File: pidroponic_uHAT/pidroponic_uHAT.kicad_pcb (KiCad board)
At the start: 2 copper layers, 65 x 30 mm, 28 parts, among them J1 GPIO_CONNECTOR, J2 1935161, J3 B4B-PH-K-S_LF__SN_, J4 B4B-PH-K-S_LF__SN_, J5 B4B-PH-K-S_LF__SN_, J6 B6B-PH-K-S_LF__SN_, J7 B4B-PH-K-S_LF__SN_, J8 TI ADS1115 Breakout, J9 B4B-PH-K-S_LF__SN_, Q1 DMG2305UX-13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

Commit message: updates over the last few evenings.
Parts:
- J2: footprint digikey-footprints:Terminal_Block_D1.3mm_P5mm -> TerminalBlock_Phoenix:TerminalBlock_Phoenix_PT-1,5-2-5.0-H_1x02_P5.00mm_Horizontal
- moved U1 10.8 mm to (133.5, 108.3)
- moved Q1 5.81 mm to (137.5, 112.6)
- moved C1 4.66 mm to (128.9, 107.3)
- moved C2 4.64 mm to (128.9, 104.0)
- moved J2 1.27 mm to (122.0, 108.8)
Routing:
- net GND: track 15.5 -> 32.1 mm, vias 1 -> 0
- net Net-(C2-Pad1): track 21.1 -> 32.1 mm
- net Net-(Q1-Pad1): track 8.00 -> 15.7 mm
- net /P12V: track 23.5 -> 17.3 mm
- net +5V: track 98.7 -> 101.7 mm
- net +3V3: track 90.4 -> 92.6 mm
- net /GPIO2_SDA1: track 35.0 -> 37.0 mm, vias 2 -> 0
- net /GPIO3_SCL1: track 35.0 -> 37.0 mm, vias 0 -> 1
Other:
- board text added: "4/27/2020 - Bryan Varner"
- board text added: "Pidroponics 1.0.8"
- board text removed: "4/23/2020 - Bryan Varner"
- board text removed: "Pidroponics 1.0.7"

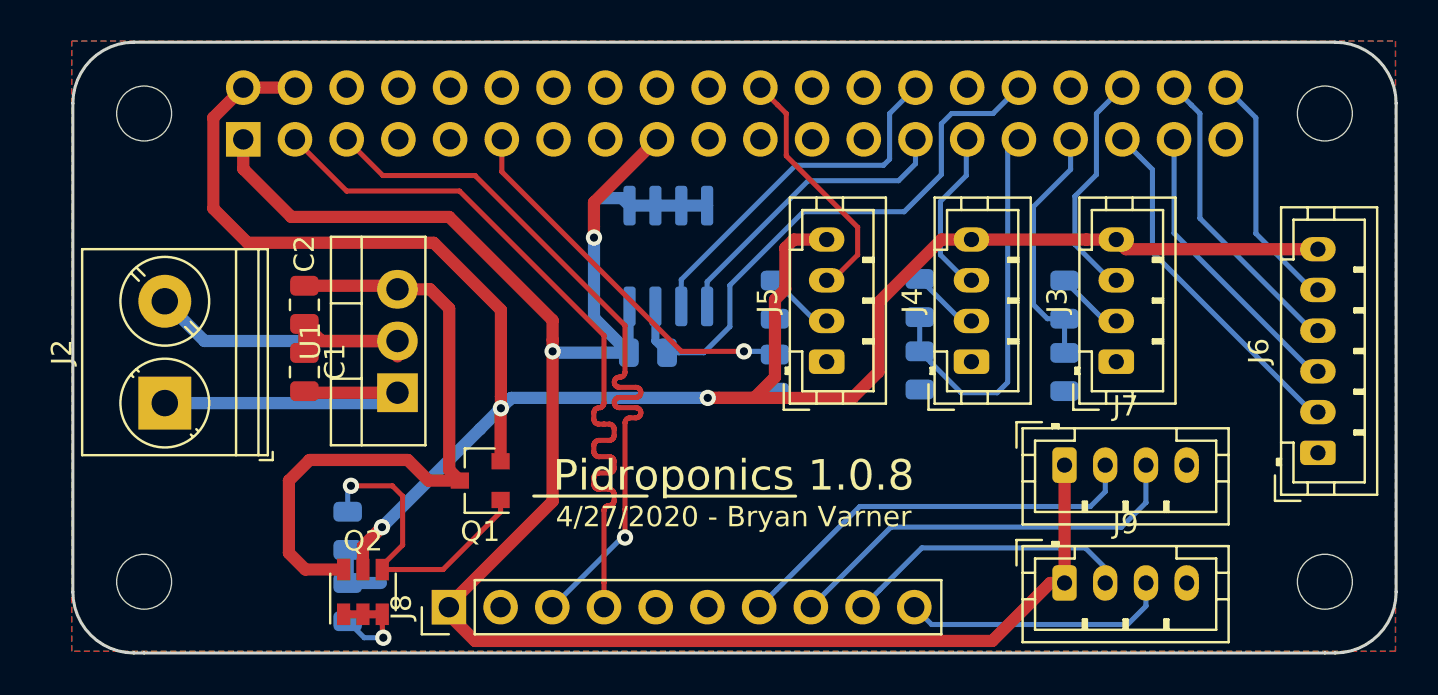
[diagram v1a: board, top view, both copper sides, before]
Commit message: Update to the uHAT, given learning new things.
* Removed the 5v linear regulator. Relays draw too much current for this to be safe. Off-board switching DC-DC buck converters are inexpensive up to 3A. Recommend using an LM2596 board.
* ADC pins configured for 3 thermistors (4.7k pullup through thermistor + filter cap) + one direct ADC feed for connecting a 3.3v analog PH Sensor
* Unified board design specs to make the 'fab' one the same as the 'homeproto'. We'll try traces this big with home proto and see where that gets us. In that vein, removed all but four vias.

General notes about this version:
* Soldering both sides of the header pins makes it possible to use those pads as vias, greatly reducing the number of 'fiddly things' you have to do.
* Removed the need for 16v 10uf caps, by dropping all the on-board voltages to 5v. Terminal block can be direct-wire soldered in place. No need for screw terminals if you don't want them.
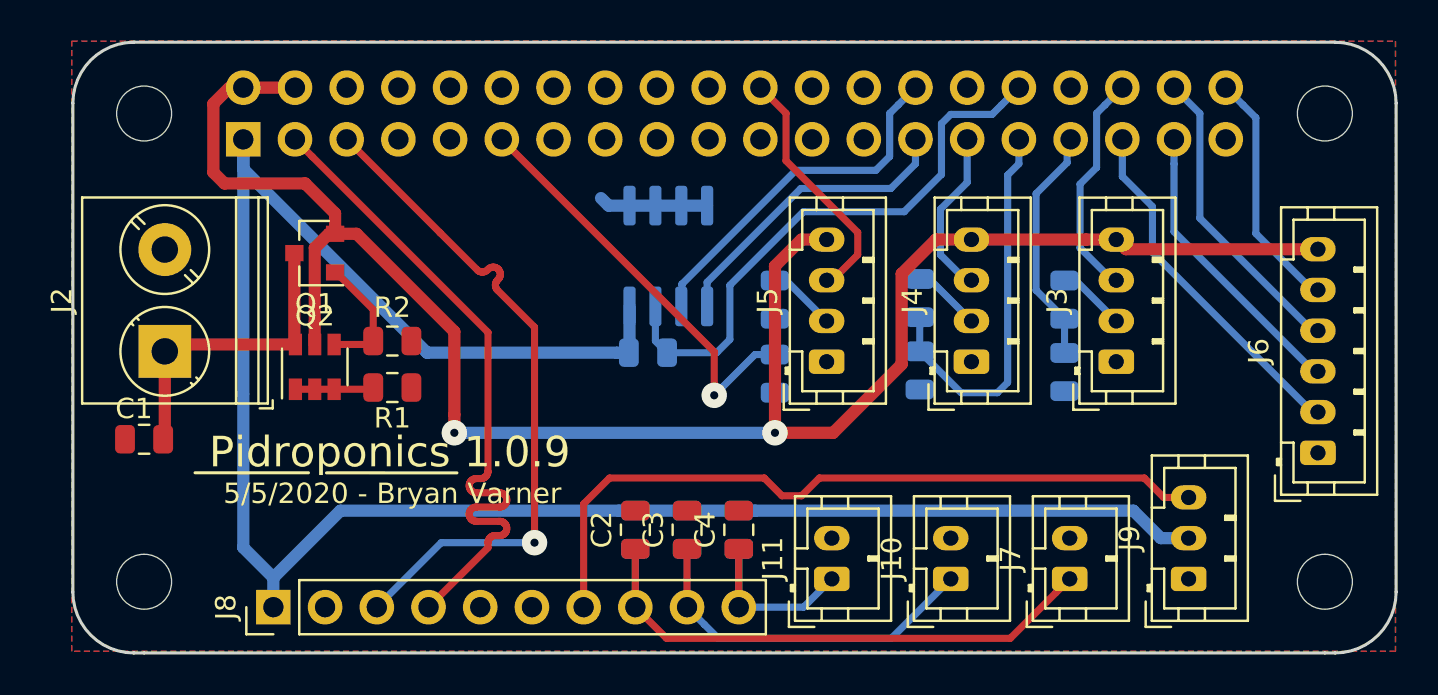
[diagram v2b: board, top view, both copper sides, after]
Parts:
- removed U1: LM7805_TO220, Package_TO_SOT_THT:TO-220-3_Vertical
- added C3: 10uf, Capacitor_SMD:C_0805_2012Metric, F.Cu at (147.7, 115.0)
- added C4: 10uf, Capacitor_SMD:C_0805_2012Metric, F.Cu at (150.2, 115.0)
- added J10: Therm 1, Connector_JST:JST_PH_B2B-PH-K_1x02_P2.00mm_Vertical, F.Cu at (160.7, 117.4)
- added J11: Therm 2, Connector_JST:JST_PH_B2B-PH-K_1x02_P2.00mm_Vertical, F.Cu at (154.8, 117.4)
- added R10: 4.7k, Resistor_SMD:R_0805_2012Metric, B.Cu at (145.2, 115.0)
- added R11: 4.7k, Resistor_SMD:R_0805_2012Metric, B.Cu at (147.7, 115.0)
- added R12: 4.7k, Resistor_SMD:R_0805_2012Metric, B.Cu at (150.2, 115.0)
- J3: value B4B-PH-K-S_LF__SN_ -> Prox 0
- J4: value B4B-PH-K-S_LF__SN_ -> Prox 1
- J5: value B4B-PH-K-S_LF__SN_ -> Prox 2
- J6: value B6B-PH-K-S_LF__SN_ -> 4 Chan Relay
- J7: value B4B-PH-K-S_LF__SN_ -> Therm 0; footprint Connector_JST:JST_PH_B4B-PH-K_1x04_P2.00mm_Vertical -> Connector_JST:JST_PH_B2B-PH-K_1x02_P2.00mm_Vertical
- J8: value TI ADS1115 Breakout -> TI ADS1115 Breakout Board
- J9: value B4B-PH-K-S_LF__SN_ -> Analog PH; footprint Connector_JST:JST_PH_B4B-PH-K_1x04_P2.00mm_Vertical -> Connector_JST:JST_PH_B3B-PH-K_1x03_P2.00mm_Vertical
- R1, R2: moved to F.Cu
- moved C2 19.7 mm to (145.2, 115.0), turned to 90 degrees
- moved Q1 13.8 mm to (129.4, 101.4)
- moved Q2 11.3 mm to (129.4, 107.0)
- moved R1 10.8 mm to (133.2, 108.0), turned to 0 degrees
- moved R2 9.58 mm to (133.2, 105.7), turned to 0 degrees
- moved J8 8.62 mm to (127.4, 118.8)
- moved C1 8.54 mm to (121.0, 110.6), turned to 180 degrees
- moved J9 6.10 mm to (172.3, 117.4), turned to 90 degrees
- moved J7 5.59 mm to (166.5, 117.4), turned to 90 degrees
- moved J2 2.54 mm to (122.0, 106.3)
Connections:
- C1 pad 1: /P12V -> /EXT5V
- C2 pad 1: Net-(C2-Pad1) -> /A1
- J1 pad 17: +3V3 -> (no net)
- J2 pad 1: /P12V -> /EXT5V
- J7 pad 1: +3V3 -> /A1
- J7 pad 2: /A0 -> GND
- J9 pad 1: +3V3 -> GND
- J9 pad 2: /A2 -> +3V3
- J9 pad 3: /A3 -> /A0
- Q1 pad 3: Net-(C2-Pad1) -> /EXT5V
- Q2 pad 6: Net-(C2-Pad1) -> /EXT5V
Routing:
- net Net-(C2-Pad1): track 32.1 -> 0.00 mm
- net GND: track 32.1 -> 5.37 mm
- net /P12V: track 17.3 -> 0.00 mm
- net /A0: track 20.7 -> 36.4 mm
- net /EXT5V: track 0.00 -> 15.4 mm
- net Net-(Q1-Pad1): track 15.7 -> 6.17 mm, vias 1 -> 0
- net /A1: track 20.4 -> 28.9 mm
- net +5V: track 101.7 -> 94.8 mm, vias 3 -> 2
- net /A2: track 14.3 -> 20.5 mm
- net +3V3: track 92.6 -> 96.9 mm, vias 2 -> 0
- net /GPIO3_SCL1: track 37.0 -> 33.6 mm
- net /GPIO2_SDA1: track 37.0 -> 34.0 mm
- net /A3: track 13.2 -> 10.9 mm
- net /GPIO17: track 20.8 -> 22.5 mm
- net Net-(Q2-Pad1): track 5.16 -> 3.86 mm, vias 1 -> 0
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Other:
- net class Default: trace_width 0.25 -> 0.35; via_dia 0.8 -> 1.25
- net class pwr: via_dia 0.8 -> 1.25
- rule trace_min: 0.2 -> 0.35
- board text added: "5/5/2020 - Bryan Varner"
- board text added: "Pidroponics 1.0.9"
- board text removed: "4/27/2020 - Bryan Varner"
- board text removed: "Pidroponics 1.0.8"

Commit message: * Refactoring device detection. * Cleaning up init. * MOving toward getting the NTC and the PH Detector setup.
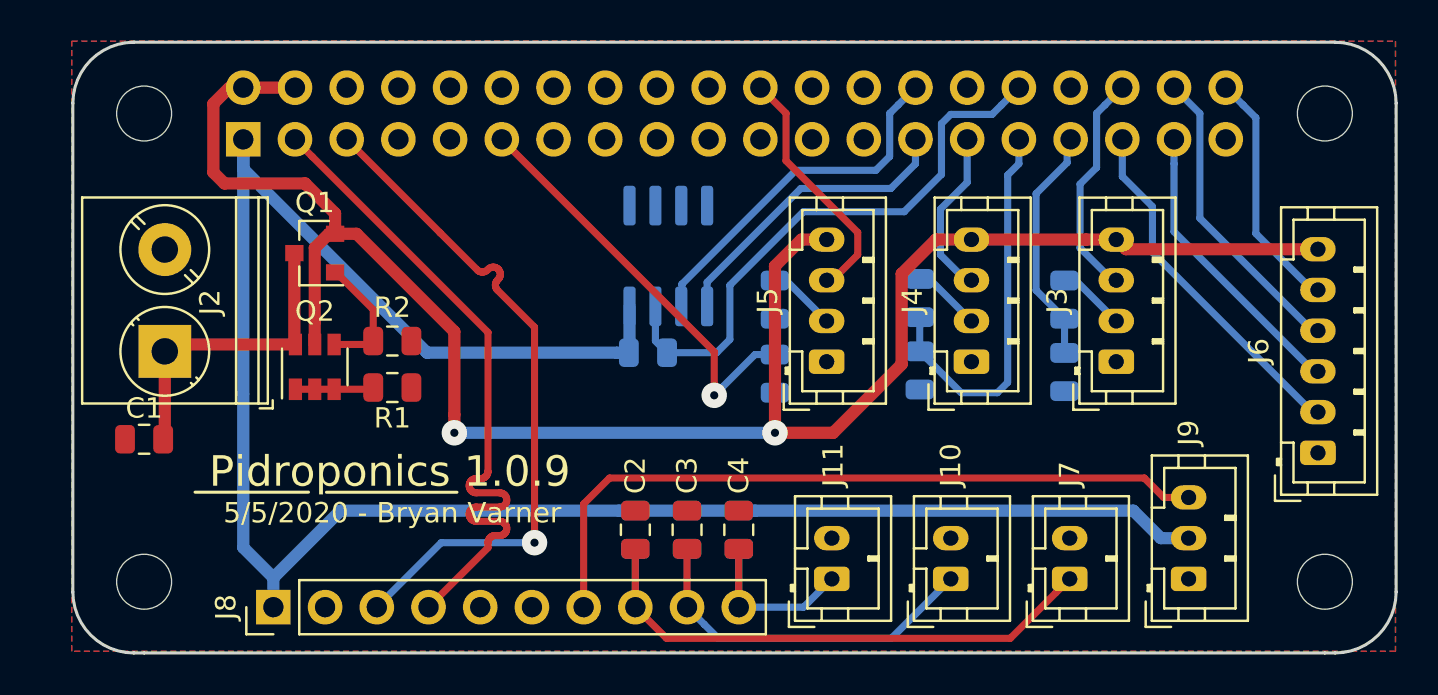
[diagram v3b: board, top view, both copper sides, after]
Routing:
- net GND: track 5.37 -> 0.00 mm
- net /A0: track 36.4 -> 35.7 mm

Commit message: Pidroponics 1.0.9 PCB & Gerbers.
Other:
- board text added: "EEPROM WP @ GPIO 12"
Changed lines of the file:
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@@
-(kicad_pcb (version 20171130) (host pcbnew 5.1.4+dfsg1-1)
+(kicad_pcb (version 20171130) (host pcbnew 5.1.5+dfsg1-2build2)
   (general
     (thickness 1.6)
-    (drawings 24)
+    (drawings 25)
     (tracks 294)
     (zones 0)
@@
     (39 F.Mask user)
     (40 Dwgs.User user)
-    (41 Cmts.User user hide)
+    (41 Cmts.User user)
     (42 Eco1.User user)
     (43 Eco2.User user)
@@
     (visible_elements FFFFFF7F)
     (pcbplotparams
-      (layerselection 0x00000_fffffffe)
-      (usegerberextensions false)
+      (layerselection 0x010fc_ffffffff)
+      (usegerberextensions true)
       (usegerberattributes false)
       (usegerberadvancedattributes false)
       (creategerberjobfile false)
-      (excludeedgelayer false)
+      (excludeedgelayer true)
       (linewidth 0.050000)
       (plotframeref false)
@@
       (psnegative false)
       (psa4output false)
-      (plotreference false)
-      (plotvalue false)
+      (plotreference true)
+      (plotvalue true)
       (plotinvisibletext false)
       (padsonsilk true)
       (subtractmaskfromsilk false)
-      (outputformat 5)
+      (outputformat 1)
       (mirror false)
-      (drillshape 1)
+      (drillshape 0)
       (scaleselection 1)
       (outputdirectory ""))
@@
     (descr "Through hole straight socket strip, 2x20, 2.54mm pitch, double cols (from Kicad 4.0.7), script generated")
     (tags "Through hole socket strip THT 2x20 2.54mm double row")
-    (fp_text reference J1 (at 2.8 -16.3) (layer B.SilkS)
+    (fp_text reference J1 (at 2.286 -0.0195) (layer B.SilkS)
       (effects (font (size 1 1) (thickness 0.15)) (justify mirror))
     )
@@
       (clearance 1.75))
   )
-  (gr_line (start 129.988986 113.171788) (end 136.399 113.1735) (layer F.SilkS) (width 0.15))
-  (gr_line (start 123.533388 113.168847) (end 129.106542 113.168847) (layer F.SilkS) (width 0.15))
-  (gr_text "5/5/2020 - Bryan Varner" (at 133.224 114.1895) (layer F.SilkS)
+  (gr_text "EEPROM WP @ GPIO 12" (at 160.3385 98.3145) (layer B.SilkS)
+    (effects (font (size 1 1) (thickness 0.15)) (justify mirror))
+  )
+  (gr_line (start 138.624986 100.598788) (end 145.035 100.6005) (layer F.SilkS) (width 0.15))
+  (gr_line (start 132.169388 100.595847) (end 137.742542 100.595847) (layer F.SilkS) (width 0.15))
+  (gr_text "5/5/2020 - Bryan Varner" (at 141.86 101.6165) (layer F.SilkS)
     (effects (font (size 1 1) (thickness 0.15)))
   )
-  (gr_text "Pidroponics 1.0.9" (at 133.097 112.1575) (layer F.SilkS)
+  (gr_text "Pidroponics 1.0.9" (at 141.733 99.5845) (layer F.SilkS)
     (effects (font (size 1.5 1.5) (thickness 0.375)))
   )
